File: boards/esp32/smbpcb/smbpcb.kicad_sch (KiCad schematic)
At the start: 53 parts, among them IC1 MiCS-6814, J1 USB_B_Micro, Q1 SUD08P06-155L, Q2 SS8050_NPN, Q3 SS8050_NPN, U1 MCP73831-2-OT, U2 TPS61200DRC, U3 ESP32-WROOM-32, U4 SSD1306, U5 BME680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

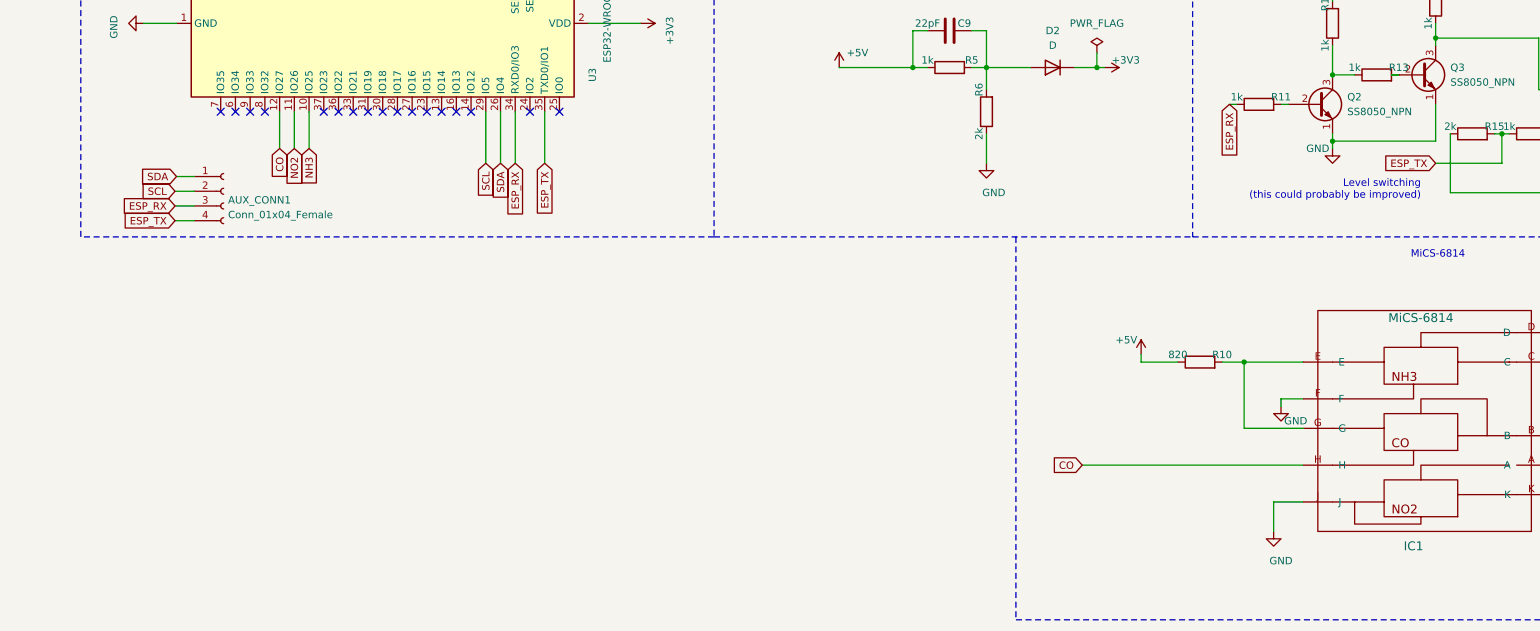
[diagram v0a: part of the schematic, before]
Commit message: pms7003 time
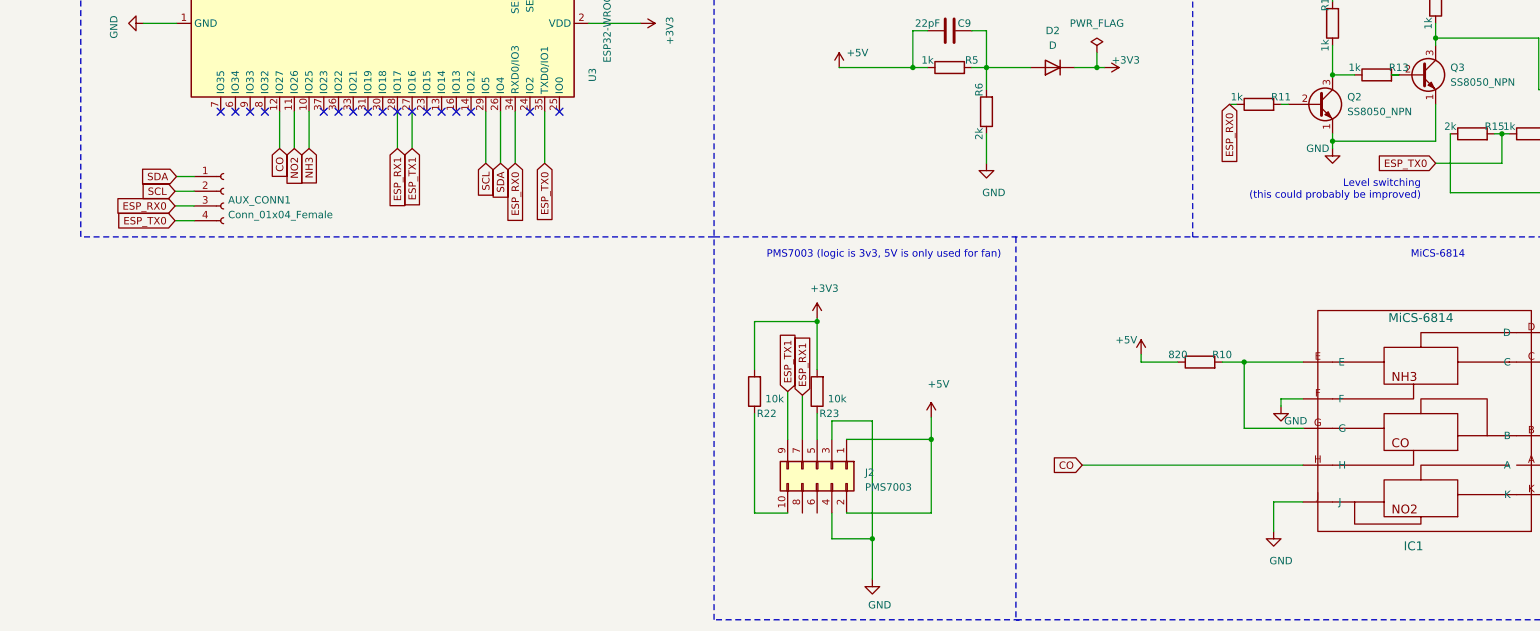
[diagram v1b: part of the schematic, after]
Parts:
- added J2: PMS7003, mics:PMS7003, symbol Connector_Generic:Conn_02x05_Odd_Even
- added R22, R23: 10k, Capacitor_SMD:C_0201_0603Metric, symbol Device:R
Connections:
- net +3V3: now also R22.2, R23.2
- net +5V: now also J2.1 (Pin_1), J2.2 (Pin_2)
- net GND: now also J2.3 (Pin_3), J2.4 (Pin_4)
- net ESP_TX1: now reaches U3.27 (IO16)
- net ESP_TX1: now also J2.9 (Pin_9)
- net ESP_RX1: now reaches U3.28 (IO17)
- net ESP_RX1: now also J2.7 (Pin_7)
- net ESP_RX renamed ESP_RX0
- net ESP_TX renamed ESP_TX0
- new net: J2.10 (Pin_10), R22.1
- new net: J2.5 (Pin_5), R23.1
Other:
- note added: "PMS7003 (logic is 3v3, 5V is only used for fan)"

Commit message: more work'
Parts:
- added AUX_CONN2, AUX_CONN3, AUX_CONN4: Conn_01x04_Female, Connector_PinHeader_1.00mm:PinHeader_1x04_P1.00mm_Vertical, symbol Connector:Conn_01x04_Female
- added C15, C16: 1nF, Capacitor_SMD:C_0201_0603Metric, symbol Device:C
- added D3, D4: PWR_LED, LED_SMD:LED_0805_2012Metric, symbol Device:LED
- added D5: D_Schottky, Diode_SMD:D_SOD-123, symbol Device:D_Schottky
- added R24, R26, R28: 470, Capacitor_SMD:C_0201_0603Metric, symbol Device:R
- added R25: 2k, Capacitor_SMD:C_0201_0603Metric, symbol Device:R
- added R27: 5.1k, Capacitor_SMD:C_0201_0603Metric, symbol Device:R
- added SW1, SW2: RESET, Button_Switch_SMD:SW_SPST_Omron_B3FS-101xP, symbol Switch:SW_Push
- 5V_IN1, EXT_BATT1: LCSC (none) -> C124375
- AUX_CONN1: LCSC (none) -> C124413
- BT1: footprint Connector_JST:JST_GH_SM02B-GHS-TB_1x02-1MP_P1.25mm_Horizontal -> Connector_JST:JST_EH_S2B-EH_1x02_P2.50mm_Horizontal; LCSC (none) -> C225399
- J1: LCSC (none) -> C404969
- J2: LCSC (none) -> C84815
- R1: value 10k -> 2k
- U4: LCSC (none) -> C91220
- U6: LCSC (none) -> C242514
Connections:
- net +3V3: now also AUX_CONN4.3 (Pin_3), R27.1
- net +5V: now also AUX_CONN2.3 (Pin_3), AUX_CONN3.3 (Pin_3), R25.2
- net CO: now also U3.6 (IO34); no longer U3.12 (IO27)
- net ESP_RX0: now also AUX_CONN1.4 (Pin_4); no longer AUX_CONN1.3 (Pin_3), R11.1
- net ESP_RX1: now also R11.1, U3.37 (IO23); no longer J2.7 (Pin_7), U3.28 (IO17)
- net ESP_TX0: now also AUX_CONN1.3 (Pin_3); no longer AUX_CONN1.4 (Pin_4), R15.2, R16.1
- net ESP_TX1: now also R15.2, R16.1, U3.36 (IO22); no longer J2.9 (Pin_9), U3.27 (IO16)
- net GND: now also AUX_CONN2.4 (Pin_4), AUX_CONN3.4 (Pin_4), AUX_CONN4.4 (Pin_4), C15.1, C16.1, SW1.2, SW2.2
- net NH3: now also U3.8 (IO32); no longer U3.10 (IO25)
- net NO2: now also U3.9 (IO33); no longer U3.11 (IO26)
- net SCL: now also AUX_CONN2.2 (Pin_2), AUX_CONN3.2 (Pin_2), AUX_CONN4.2 (Pin_2)
- net SDA: now also AUX_CONN2.1 (Pin_1), AUX_CONN3.1 (Pin_1), AUX_CONN4.1 (Pin_1)
- net at C1.1, D1.2 (A), Q1.1 (G)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: now also D5.2 (A), R28.2; no longer 5V_IN1.1 (Pin_1), J1.1 (VBUS)
- net at C5.1, D1.1 (K): now also D3.1 (K)
- net IO0: now reaches U3.25 (IO0)
- net IO0: now also R24.2, R27.2
- net EN: now reaches U3.3 (EN)
- net EN: now also R26.2
- net at U1.1 (STAT): now also D4.1 (K)
- new net: 5V_IN1.1 (Pin_1), D5.1 (K), J1.1 (VBUS)
- new net: D3.2 (A), R25.1
- new net: C15.2, R24.1, SW1.1
- new net: D4.2 (A), R28.1
- new net: C16.2, R26.1, SW2.1
- new net ESP_RX2: J2.7 (Pin_7), U3.28 (IO17)
- new net ESP_TX2: J2.9 (Pin_9), U3.27 (IO16)
- no-connect marks 32 -> 25
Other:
- note added: "2k resistor = 500mA charge current"
- note added: "Flashing / Bootmode selection"
- note added: "TODO probably include reset /io0 pins"
- note removed: "100mA charging, change R1 to 2.7kOhms for 500mA"
- note removed: "PMS7003: TODO probably not that hard gotta make custom footprint/schematic tho"
- moved on the sheet: AUX_CONN1, BT1, C2

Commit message: ordering dis
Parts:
- C1, C2, C3: LCSC C29823 -> C17673
- R1: footprint Capacitor_SMD:C_1206_3216Metric -> Capacitor_SMD:C_0201_0603Metric; LCSC C17902 -> C25590
- R10: LCSC C23253 -> C25259
- R15, R25, R6: LCSC C4190 -> C25590
- R17, R18: footprint Capacitor_SMD:C_1206_3216Metric -> Capacitor_SMD:C_0805_2012Metric; LCSC C17936 -> C64354
- R22, R23, R4, R7, R8, R9: footprint Capacitor_SMD:C_0201_0603Metric -> Capacitor_SMD:C_0805_2012Metric; LCSC C25804 -> C269724
- R27: footprint Capacitor_SMD:C_0201_0603Metric -> Capacitor_SMD:C_0805_2012Metric; LCSC C23186 -> C328405
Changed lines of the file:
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@@
       (effects (font (size 1.27 1.27)) (justify left))
     )
-    (property "Footprint" "Capacitor_SMD:C_1206_3216Metric" (id 2) (at 49.657 66.04 90)
+    (property "Footprint" "Capacitor_SMD:C_0201_0603Metric" (id 2) (at 49.657 66.04 90)
       (effects (font (size 1.27 1.27)) hide)
     )
@@
       (effects (font (size 1.27 1.27)) hide)
     )
-    (property "LCSC" "C17902" (id 4) (at 51.435 66.04 0)
+    (property "LCSC" "C25590" (id 4) (at 51.435 66.04 0)
       (effects (font (size 1.27 1.27)) hide)
     )
@@
       (effects (font (size 1.27 1.27)) (justify left))
     )
-    (property "Footprint" "Capacitor_SMD:C_0201_0603Metric" (id 2) (at 84.582 32.385 90)
+    (property "Footprint" "Capacitor_SMD:C_0805_2012Metric" (id 2) (at 84.582 32.385 90)
       (effects (font (size 1.27 1.27)) hide)
     )
@@
       (effects (font (size 1.27 1.27)) hide)
     )
-    (property "LCSC" "C25804" (id 4) (at 86.36 32.385 0)
+    (property "LCSC" "C269724" (id 4) (at 86.36 32.385 0)
       (effects (font (size 1.27 1.27)) hide)
     )
@@
       (effects (font (size 1.27 1.27)) hide)
     )
-    (property "LCSC" " C4190" (id 4) (at 189.23 48.26 0)
+    (property "LCSC" "C25590" (id 4) (at 189.23 48.26 0)
       (effects (font (size 1.27 1.27)) hide)
     )
@@
       (effects (font (size 1.27 1.27)) (justify left))
     )
-    (property "Footprint" "Capacitor_SMD:C_0201_0603Metric" (id 2) (at 218.567 123.825 90)
+    (property "Footprint" "Capacitor_SMD:C_0805_2012Metric" (id 2) (at 218.567 123.825 90)
       (effects (font (size 1.27 1.27)) hide)
     )
@@
       (effects (font (size 1.27 1.27)) hide)
     )
-    (property "LCSC" "C23186" (id 4) (at 220.345 123.825 0)
+    (property "LCSC" "C328405" (id 4) (at 220.345 123.825 0)
       (effects (font (size 1.27 1.27)) hide)
     )
@@
       (effects (font (size 1.27 1.27)) (justify left))
     )
-    (property "Footprint" "Capacitor_SMD:C_0201_0603Metric" (id 2) (at 242.443 179.07 90)
+    (property "Footprint" "Capacitor_SMD:C_0805_2012Metric" (id 2) (at 242.443 179.07 90)
       (effects (font (size 1.27 1.27)) hide)
     )
@@
       (effects (font (size 1.27 1.27)) hide)
     )
-    (property "LCSC" "C25804" (id 4) (at 240.665 179.07 0)
+    (property "LCSC" "C269724" (id 4) (at 240.665 179.07 0)
       (effects (font (size 1.27 1.27)) hide)
     )
@@
       (effects (font (size 1.27 1.27)) (justify left))
     )
-    (property "Footprint" "Capacitor_SMD:C_0201_0603Metric" (id 2) (at 253.238 179.07 90)
+    (property "Footprint" "Capacitor_SMD:C_0805_2012Metric" (id 2) (at 253.238 179.07 90)
       (effects (font (size 1.27 1.27)) hide)
     )
@@
       (effects (font (size 1.27 1.27)) hide)
     )
-    (property "LCSC" "C25804" (id 4) (at 251.46 179.07 0)
+    (property "LCSC" "C269724" (id 4) (at 251.46 179.07 0)
       (effects (font (size 1.27 1.27)) hide)
     )
@@
       (effects (font (size 1.27 1.27)) (justify left))
     )
-    (property "Footprint" "Capacitor_SMD:C_0201_0603Metric" (id 2) (at 256.54 65.278 90)
+    (property "Footprint" "Capacitor_SMD:C_0805_2012Metric" (id 2) (at 256.54 65.278 90)
       (effects (font (size 1.27 1.27)) hide)
     )
@@
       (effects (font (size 1.27 1.27)) hide)
     )
-    (property "LCSC" "C25804" (id 4) (at 256.54 63.5 0)
+    (property "LCSC" "C269724" (id 4) (at 256.54 63.5 0)
       (effects (font (size 1.27 1.27)) hide)
     )
@@
       (effects (font (size 1.27 1.27)) (justify left))
     )
-    (property "Footprint" "Capacitor_SMD:C_0201_0603Metric" (id 2) (at 279.4 70.358 90)
+    (property "Footprint" "Capacitor_SMD:C_0805_2012Metric" (id 2) (at 279.4 70.358 90)
       (effects (font (size 1.27 1.27)) hide)
     )
@@
       (effects (font (size 1.27 1.27)) hide)
     )
-    (property "LCSC" "C25804" (id 4) (at 279.4 68.58 0)
+    (property "LCSC" "C269724" (id 4) (at 279.4 68.58 0)
       (effects (font (size 1.27 1.27)) hide)
     )
@@
       (effects (font (size 1.27 1.27)) hide)
     )
-    (property "LCSC" " C4190" (id 4) (at 280.67 130.81 0)
+    (property "LCSC" "C25590" (id 4) (at 280.67 130.81 0)
       (effects (font (size 1.27 1.27)) hide)
     )
@@
       (effects (font (size 1.27 1.27)) (justify left))
     )
-    (property "Footprint" "Capacitor_SMD:C_0201_0603Metric" (id 2) (at 284.48 74.168 90)
+    (property "Footprint" "Capacitor_SMD:C_0805_2012Metric" (id 2) (at 284.48 74.168 90)
       (effects (font (size 1.27 1.27)) hide)
     )
@@
       (effects (font (size 1.27 1.27)) hide)
     )
-    (property "LCSC" "C25804" (id 4) (at 284.48 72.39 0)
+    (property "LCSC" "C269724" (id 4) (at 284.48 72.39 0)
       (effects (font (size 1.27 1.27)) hide)
     )
@@
       (effects (font (size 1.27 1.27)) hide)
     )
-    (property "LCSC" "C23253" (id 4) (at 317.5 173.99 0)
+    (property "LCSC" " C25259" (id 4) (at 317.5 173.99 0)
       (effects (font (size 1.27 1.27)) hide)
     )
@@
       (effects (font (size 1.27 1.27)) hide)
     )
-    (property "LCSC" " C4190" (id 4) (at 364.49 134.62 0)
+    (property "LCSC" "C25590" (id 4) (at 364.49 134.62 0)
       (effects (font (size 1.27 1.27)) hide)
     )
@@
       (effects (font (size 1.27 1.27)) (justify left))
     )
-    (property "Footprint" "Capacitor_SMD:C_1206_3216Metric" (id 2) (at 380.492 68.58 90)
+    (property "Footprint" "Capacitor_SMD:C_0805_2012Metric" (id 2) (at 380.492 68.58 90)
       (effects (font (size 1.27 1.27)) hide)
     )
@@
       (effects (font (size 1.27 1.27)) hide)
     )
-    (property "LCSC" "C17936" (id 4) (at 382.27 68.58 0)
+    (property "LCSC" "C64354" (id 4) (at 382.27 68.58 0)
       (effects (font (size 1.27 1.27)) hide)
     )
@@
       (effects (font (size 1.27 1.27)) (justify left))
     )
-    (property "Footprint" "Capacitor_SMD:C_1206_3216Metric" (id 2) (at 389.382 68.58 90)
+    (property "Footprint" "Capacitor_SMD:C_0805_2012Metric" (id 2) (at 389.382 68.58 90)
       (effects (font (size 1.27 1.27)) hide)
     )
@@
       (effects (font (size 1.27 1.27)) hide)
     )
-    (property "LCSC" "C17936" (id 4) (at 391.16 68.58 0)
+    (property "LCSC" "C64354" (id 4) (at 391.16 68.58 0)
       (effects (font (size 1.27 1.27)) hide)
     )
@@
       (effects (font (size 1.27 1.27)) hide)
     )
-    (property "LCSC" "C29823" (id 4) (at 40.005 60.325 0)
+    (property "LCSC" "C17673" (id 4) (at 40.005 60.325 0)
       (effects (font (size 1.27 1.27)) hide)
     )
@@
       (effects (font (size 1.27 1.27)) hide)
     )
-    (property "LCSC" "C29823" (id 4) (at 81.28 60.96 0)
+    (property "LCSC" "C17673" (id 4) (at 81.28 60.96 0)
       (effects (font (size 1.27 1.27)) hide)
     )
@@
       (effects (font (size 1.27 1.27)) hide)
     )
-    (property "LCSC" "C29823" (id 4) (at 123.825 55.88 0)
+    (property "LCSC" "C17673" (id 4) (at 123.825 55.88 0)
       (effects (font (size 1.27 1.27)) hide)
     )
@@
     )
     (path "/1b571b92-9dce-4ad4-9cab-18393b9c169c"
-      (reference "R1") (unit 1) (value "2k") (footprint "Capacitor_SMD:C_1206_3216Metric")
+      (reference "R1") (unit 1) (value "2k") (footprint "Capacitor_SMD:C_0201_0603Metric")
     )
     (path "/7ce0cdba-4ded-4b53-b063-437a459b9541"
@@
     )
     (path "/b535da43-399b-4889-b94c-4dc9d1e79e67"
-      (reference "R4") (unit 1) (value "10k") (footprint "Capacitor_SMD:C_0201_0603Metric")
+      (reference "R4") (unit 1) (value "10k") (footprint "Capacitor_SMD:C_0805_2012Metric")
     )
     (path "/99d10c75-af0b-4f7f-93e6-5f4d550f82e7"
@@
     )
     (path "/1c4a4bf4-60ac-4b19-a35c-5bfef48f0c90"
-      (reference "R7") (unit 1) (value "10k") (footprint "Capacitor_SMD:C_0201_0603Metric")
+      (reference "R7") (unit 1) (value "10k") (footprint "Capacitor_SMD:C_0805_2012Metric")
     )
     (path "/b8cece64-c0e6-4256-afcc-60fe147c2735"
-      (reference "R8") (unit 1) (value "10k") (footprint "Capacitor_SMD:C_0201_0603Metric")
+      (reference "R8") (unit 1) (value "10k") (footprint "Capacitor_SMD:C_0805_2012Metric")
     )
     (path "/77b7447c-2434-4b36-94ea-f2ab49d7177e"
-      (reference "R9") (unit 1) (value "10k") (footprint "Capacitor_SMD:C_0201_0603Metric")
+      (reference "R9") (unit 1) (value "10k") (footprint "Capacitor_SMD:C_0805_2012Metric")
     )
     (path "/75f238b5-4058-47cc-8c02-f8ccf5f28c0d"
@@
     )
     (path "/48ecb9b2-9c9c-42ac-9e9f-cab25ac716a7"
-      (reference "R17") (unit 1) (value "4.7k") (footprint "Capacitor_SMD:C_1206_3216Metric")
+      (reference "R17") (unit 1) (value "4.7k") (footprint "Capacitor_SMD:C_0805_2012Metric")
     )
     (path "/33b47815-c87d-4054-811e-8a180ff4b4a5"
-      (reference "R18") (unit 1) (value "4.7k") (footprint "Capacitor_SMD:C_1206_3216Metric")
+      (reference "R18") (unit 1) (value "4.7k") (footprint "Capacitor_SMD:C_0805_2012Metric")
     )
     (path "/0966f30f-63a6-408e-948c-ee9c9d9c86cb"
@@
     )
     (path "/026bd94d-e02a-47ba-bb0a-a81a59b74051"
-      (reference "R22") (unit 1) (value "10k") (footprint "Capacitor_SMD:C_0201_0603Metric")
+      (reference "R22") (unit 1) (value "10k") (footprint "Capacitor_SMD:C_0805_2012Metric")
     )
     (path "/860bb2e1-7ddb-481a-9248-8da6b7b007b5"
-      (reference "R23") (unit 1) (value "10k") (footprint "Capacitor_SMD:C_0201_0603Metric")
+      (reference "R23") (unit 1) (value "10k") (footprint "Capacitor_SMD:C_0805_2012Metric")
     )
     (path "/967168fb-e7d3-45f6-8cc6-1e9e96844b85"
@@
     )
     (path "/7f6c1586-2cfd-4167-bcf0-c88517a26078"
-      (reference "R27") (unit 1) (value "5.1k") (footprint "Capacitor_SMD:C_0201_0603Metric")
+      (reference "R27") (unit 1) (value "5.1k") (footprint "Capacitor_SMD:C_0805_2012Metric")
     )
     (path "/b69ae685-e389-4de0-86e5-81c4fbf5127d"

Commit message: ordering dis
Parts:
- C1, C2, C3: LCSC C17673 -> C412617
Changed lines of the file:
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@@
       (effects (font (size 1.27 1.27)) hide)
     )
-    (property "LCSC" "C17673" (id 4) (at 40.005 60.325 0)
+    (property "LCSC" "C412617" (id 4) (at 40.005 60.325 0)
       (effects (font (size 1.27 1.27)) hide)
     )
@@
       (effects (font (size 1.27 1.27)) hide)
     )
-    (property "LCSC" "C17673" (id 4) (at 81.28 60.96 0)
+    (property "LCSC" "C412617" (id 4) (at 81.28 60.96 0)
       (effects (font (size 1.27 1.27)) hide)
     )
@@
       (effects (font (size 1.27 1.27)) hide)
     )
-    (property "LCSC" "C17673" (id 4) (at 123.825 55.88 0)
+    (property "LCSC" "C412617" (id 4) (at 123.825 55.88 0)
       (effects (font (size 1.27 1.27)) hide)
     )
